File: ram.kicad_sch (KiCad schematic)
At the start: 56 parts

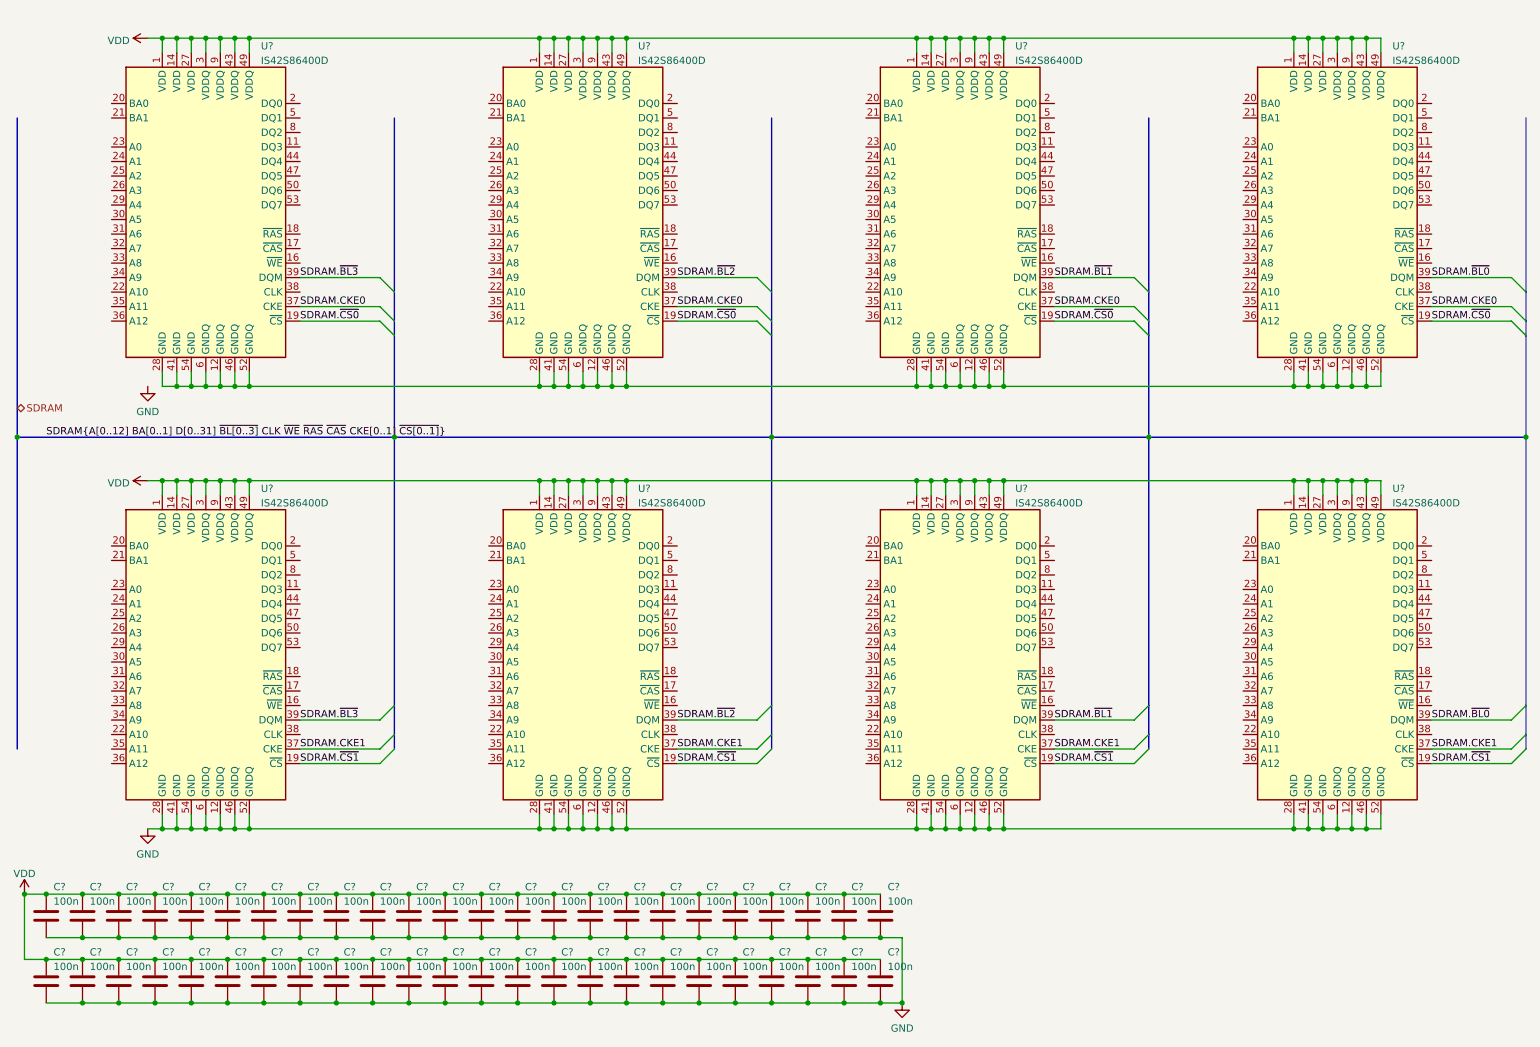
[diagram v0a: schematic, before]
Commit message: Complete wiring of SDRAM.
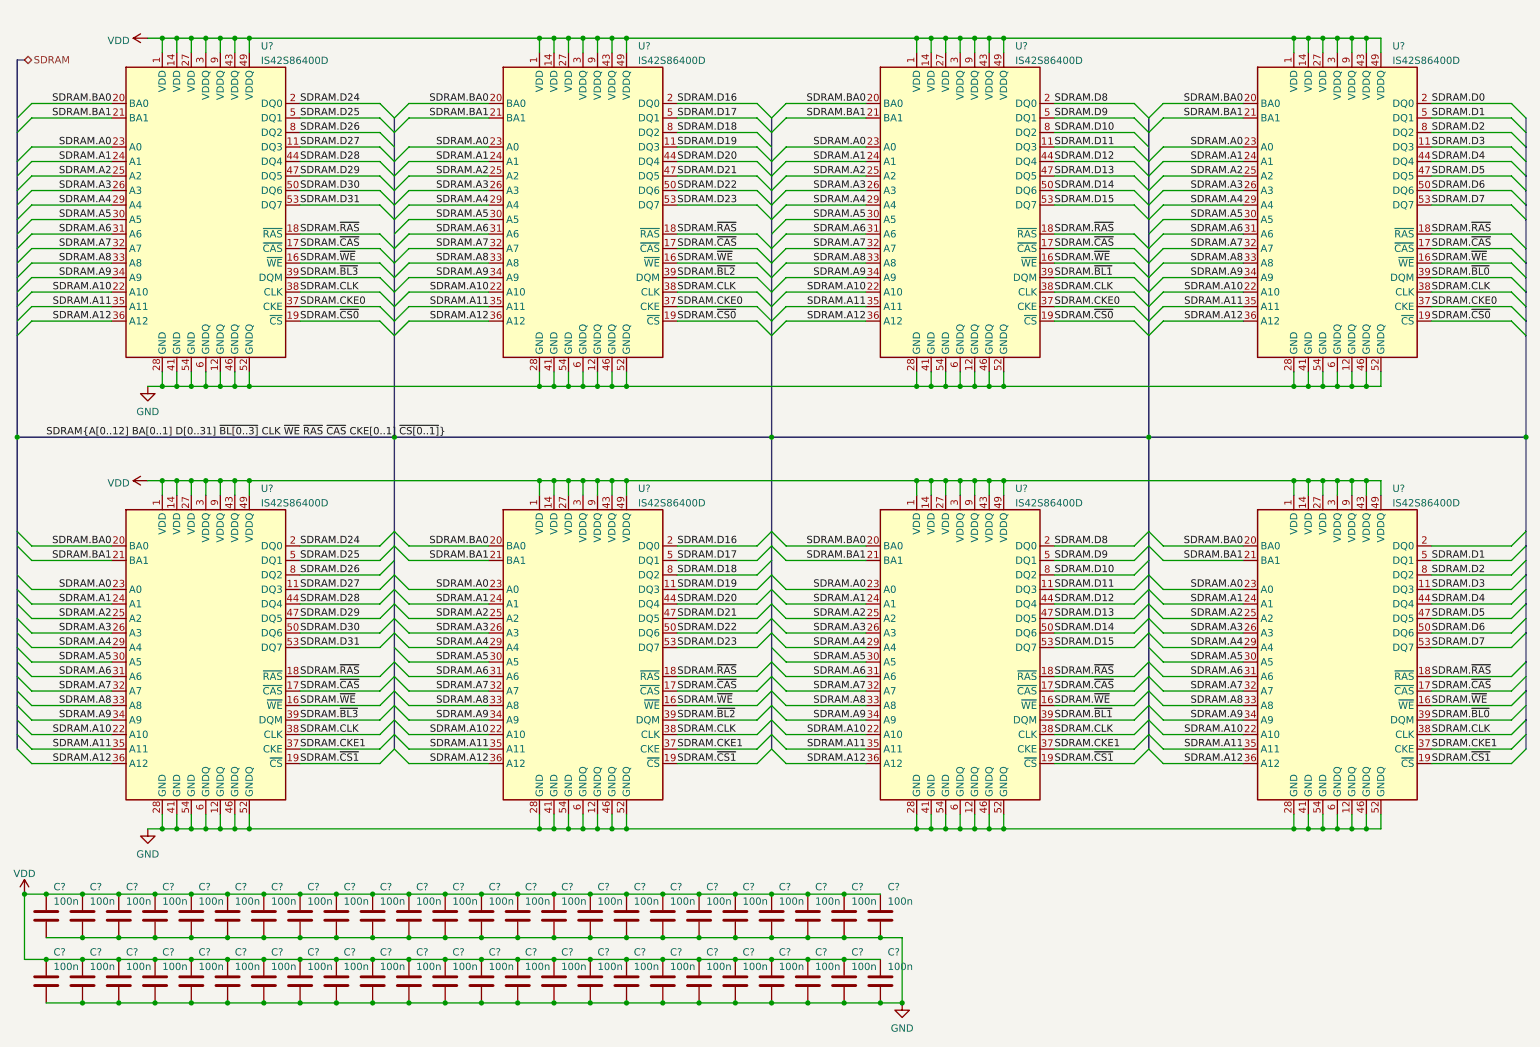
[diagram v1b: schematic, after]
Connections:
- net GND: now also U?.12 (GNDQ), U?.12 (GNDQ), U?.12 (GNDQ), U?.12 (GNDQ), U?.28 (GND), U?.28 (GND), U?.28 (GND), U?.28 (GND), U?.41 (GND), U?.41 (GND), U?.41 (GND), U?.41 (GND), U?.46 (GNDQ), U?.46 (GNDQ), U?.46 (GNDQ), U?.46 (GNDQ), U?.52 (GNDQ), U?.52 (GNDQ), U?.52 (GNDQ), U?.52 (GNDQ), U?.54 (GND), U?.54 (GND), U?.54 (GND), U?.54 (GND), U?.6 (GNDQ), U?.6 (GNDQ), U?.6 (GNDQ), U?.6 (GNDQ)
- net SDRAM.D11: now reaches U?.11 (DQ3)
- net SDRAM.D11: now also U?.11 (DQ3)
- net SDRAM.~{WE}: now reaches U?.16 (~{WE})
- net SDRAM.~{WE}: now also U?.16 (~{WE}), U?.16 (~{WE}), U?.16 (~{WE}), U?.16 (~{WE}), U?.16 (~{WE}), U?.16 (~{WE}), U?.16 (~{WE})
- net SDRAM.~{CAS}: now reaches U?.17 (~{CAS})
- net SDRAM.~{CAS}: now also U?.17 (~{CAS}), U?.17 (~{CAS}), U?.17 (~{CAS}), U?.17 (~{CAS}), U?.17 (~{CAS}), U?.17 (~{CAS}), U?.17 (~{CAS})
- net SDRAM.~{RAS}: now reaches U?.18 (~{RAS})
- net SDRAM.~{RAS}: now also U?.18 (~{RAS}), U?.18 (~{RAS}), U?.18 (~{RAS}), U?.18 (~{RAS}), U?.18 (~{RAS}), U?.18 (~{RAS}), U?.18 (~{RAS})
- net SDRAM.D8: now reaches U?.2 (DQ0)
- net SDRAM.D8: now also U?.2 (DQ0)
- net SDRAM.BA0: now reaches U?.20 (BA0)
- net SDRAM.BA0: now also U?.20 (BA0), U?.20 (BA0), U?.20 (BA0), U?.20 (BA0), U?.20 (BA0), U?.20 (BA0), U?.20 (BA0)
- net SDRAM.BA1: now reaches U?.21 (BA1)
- net SDRAM.BA1: now also U?.21 (BA1), U?.21 (BA1), U?.21 (BA1), U?.21 (BA1), U?.21 (BA1), U?.21 (BA1), U?.21 (BA1)
- net SDRAM.A10: now reaches U?.22 (A10)
- net SDRAM.A10: now also U?.22 (A10), U?.22 (A10), U?.22 (A10), U?.22 (A10), U?.22 (A10), U?.22 (A10), U?.22 (A10)
- net SDRAM.A0: now reaches U?.23 (A0)
- net SDRAM.A0: now also U?.23 (A0), U?.23 (A0), U?.23 (A0), U?.23 (A0), U?.23 (A0), U?.23 (A0), U?.23 (A0)
- net SDRAM.A1: now reaches U?.24 (A1)
- net SDRAM.A1: now also U?.24 (A1), U?.24 (A1), U?.24 (A1), U?.24 (A1), U?.24 (A1), U?.24 (A1), U?.24 (A1)
- net SDRAM.A2: now reaches U?.25 (A2)
- net SDRAM.A2: now also U?.25 (A2), U?.25 (A2), U?.25 (A2), U?.25 (A2), U?.25 (A2), U?.25 (A2), U?.25 (A2)
- net SDRAM.A3: now reaches U?.26 (A3)
- net SDRAM.A3: now also U?.26 (A3), U?.26 (A3), U?.26 (A3), U?.26 (A3), U?.26 (A3), U?.26 (A3), U?.26 (A3)
- net SDRAM.A4: now reaches U?.29 (A4)
- net SDRAM.A4: now also U?.29 (A4), U?.29 (A4), U?.29 (A4), U?.29 (A4), U?.29 (A4), U?.29 (A4), U?.29 (A4)
- net SDRAM.A5: now reaches U?.30 (A5)
- net SDRAM.A5: now also U?.30 (A5), U?.30 (A5), U?.30 (A5), U?.30 (A5), U?.30 (A5), U?.30 (A5), U?.30 (A5)
- net SDRAM.A6: now reaches U?.31 (A6)
- net SDRAM.A6: now also U?.31 (A6), U?.31 (A6), U?.31 (A6), U?.31 (A6), U?.31 (A6), U?.31 (A6), U?.31 (A6)
- net SDRAM.A7: now reaches U?.32 (A7)
- net SDRAM.A7: now also U?.32 (A7), U?.32 (A7), U?.32 (A7), U?.32 (A7), U?.32 (A7), U?.32 (A7), U?.32 (A7)
- net SDRAM.A8: now reaches U?.33 (A8)
- net SDRAM.A8: now also U?.33 (A8), U?.33 (A8), U?.33 (A8), U?.33 (A8), U?.33 (A8), U?.33 (A8), U?.33 (A8)
- net SDRAM.A9: now reaches U?.34 (A9)
- net SDRAM.A9: now also U?.34 (A9), U?.34 (A9), U?.34 (A9), U?.34 (A9), U?.34 (A9), U?.34 (A9), U?.34 (A9)
- net SDRAM.A11: now reaches U?.35 (A11)
- net SDRAM.A11: now also U?.35 (A11), U?.35 (A11), U?.35 (A11), U?.35 (A11), U?.35 (A11), U?.35 (A11), U?.35 (A11)
- net SDRAM.A12: now reaches U?.36 (A12)
- net SDRAM.A12: now also U?.36 (A12), U?.36 (A12), U?.36 (A12), U?.36 (A12), U?.36 (A12), U?.36 (A12), U?.36 (A12)
- net SDRAM.CLK: now reaches U?.38 (CLK)
- net SDRAM.CLK: now also U?.38 (CLK), U?.38 (CLK), U?.38 (CLK), U?.38 (CLK), U?.38 (CLK), U?.38 (CLK), U?.38 (CLK)
- net SDRAM.D12: now reaches U?.44 (DQ4)
- net SDRAM.D12: now also U?.44 (DQ4)
- net SDRAM.D13: now reaches U?.47 (DQ5)
- net SDRAM.D13: now also U?.47 (DQ5)
- net SDRAM.D9: now reaches U?.5 (DQ1)
- net SDRAM.D9: now also U?.5 (DQ1)
- net SDRAM.D14: now reaches U?.50 (DQ6)
- net SDRAM.D14: now also U?.50 (DQ6)
- net SDRAM.D15: now reaches U?.53 (DQ7)
- net SDRAM.D15: now also U?.53 (DQ7)
- net SDRAM.D10: now reaches U?.8 (DQ2)
- net SDRAM.D10: now also U?.8 (DQ2)
- net SDRAM.D19: now reaches U?.11 (DQ3)
- net SDRAM.D19: now also U?.11 (DQ3)
- net SDRAM.D16: now reaches U?.2 (DQ0)
- net SDRAM.D16: now also U?.2 (DQ0)
- net SDRAM.D20: now reaches U?.44 (DQ4)
- net SDRAM.D20: now also U?.44 (DQ4)
- net SDRAM.D21: now reaches U?.47 (DQ5)
- net SDRAM.D21: now also U?.47 (DQ5)
- net SDRAM.D17: now reaches U?.5 (DQ1)
- net SDRAM.D17: now also U?.5 (DQ1)
- net SDRAM.D22: now reaches U?.50 (DQ6)
- net SDRAM.D22: now also U?.50 (DQ6)
- net SDRAM.D23: now reaches U?.53 (DQ7)
- net SDRAM.D23: now also U?.53 (DQ7)
- net SDRAM.D18: now reaches U?.8 (DQ2)
- net SDRAM.D18: now also U?.8 (DQ2)
- net SDRAM.D27: now reaches U?.11 (DQ3)
- net SDRAM.D27: now also U?.11 (DQ3)
- net SDRAM.D24: now reaches U?.2 (DQ0)
- net SDRAM.D24: now also U?.2 (DQ0)
- net SDRAM.D28: now reaches U?.44 (DQ4)
- net SDRAM.D28: now also U?.44 (DQ4)
- net SDRAM.D29: now reaches U?.47 (DQ5)
- net SDRAM.D29: now also U?.47 (DQ5)
- net SDRAM.D25: now reaches U?.5 (DQ1)
- net SDRAM.D25: now also U?.5 (DQ1)
- net SDRAM.D30: now reaches U?.50 (DQ6)
- net SDRAM.D30: now also U?.50 (DQ6)
- net SDRAM.D31: now reaches U?.53 (DQ7)
- net SDRAM.D31: now also U?.53 (DQ7)
- net SDRAM.D26: now reaches U?.8 (DQ2)
- net SDRAM.D26: now also U?.8 (DQ2)
- net SDRAM.D3: now reaches U?.11 (DQ3)
- net SDRAM.D3: now also U?.11 (DQ3)
- net SDRAM.D4: now reaches U?.44 (DQ4)
- net SDRAM.D4: now also U?.44 (DQ4)
- net SDRAM.D5: now reaches U?.47 (DQ5)
- net SDRAM.D5: now also U?.47 (DQ5)
- net SDRAM.D1: now reaches U?.5 (DQ1)
- net SDRAM.D1: now also U?.5 (DQ1)
- net SDRAM.D6: now reaches U?.50 (DQ6)
- net SDRAM.D6: now also U?.50 (DQ6)
- net SDRAM.D7: now reaches U?.53 (DQ7)
- net SDRAM.D7: now also U?.53 (DQ7)
- net SDRAM.D2: now reaches U?.8 (DQ2)
- net SDRAM.D2: now also U?.8 (DQ2)
- net SDRAM.D0: now reaches U?.2 (DQ0)

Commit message: Add SD card connector.
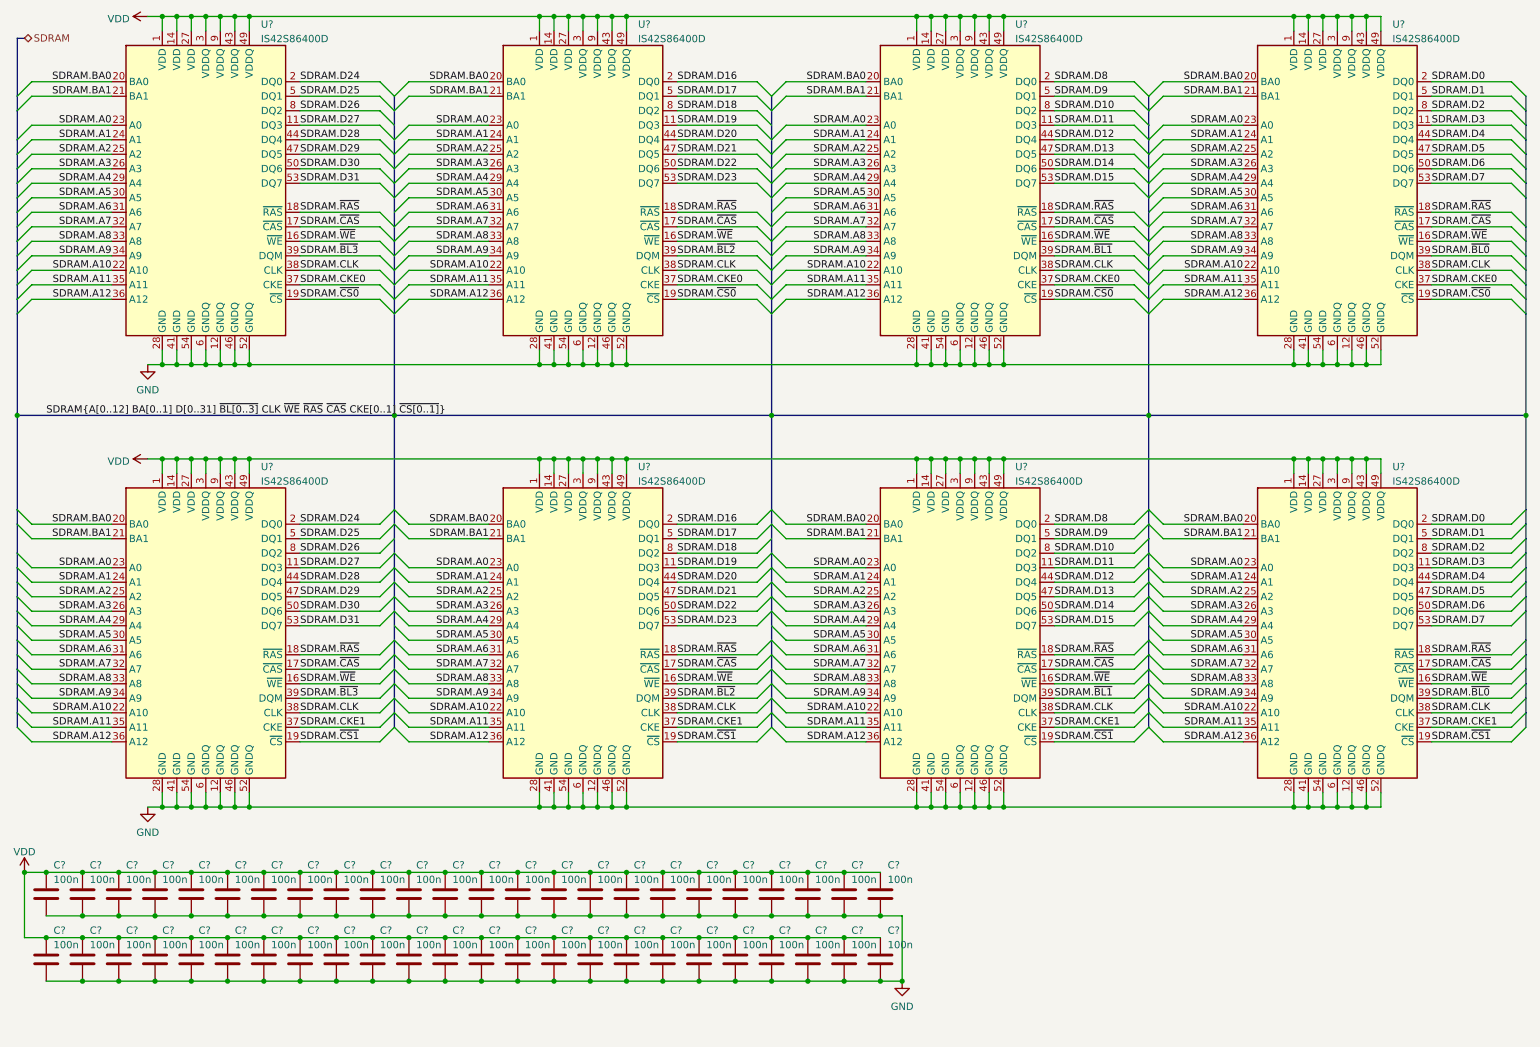
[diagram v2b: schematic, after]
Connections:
- net SDRAM.D0: now also U?.2 (DQ0)
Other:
- moved on the sheet: C?, U?

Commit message: Add power supply.
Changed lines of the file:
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@@
     (pin "2")
   )
-  (symbol (lib_id "marco-ram-board:IS42S86400D") (at 181.61 52.07 0) (unit 1)
-    (in_bom yes) (on_board yes) (fields_autoplaced)
-    (property "Reference" "U?" (id 0) (at 191.2494 21.7002 0)
-      (effects (font (size 1.27 1.27)) (justify left))
-    )
-    (property "Value" "IS42S86400D" (id 1) (at 191.2494 24.2371 0)
-      (effects (font (size 1.27 1.27)) (justify left))
-    )
+  (symbol (lib_name "IS42S86400D_4") (lib_id "marco-ram-board:IS42S86400D") (at 181.61 52.07 0) (unit 1)
+    (in_bom yes) (on_board yes)
+    (property "Reference" "U?" (id 0) (at 181.61 50.8031 0))
+    (property "Value" "IS42S86400D" (id 1) (at 181.61 53.34 0))
     (property "Footprint" "Package_SO:TSOP-II-54_22.2x10.16mm_P0.8mm" (id 2) (at 181.61 81.28 0)
       (effects (font (size 1.27 1.27)) hide)
@@
     (pin "2")
   )
-  (symbol (lib_id "marco-ram-board:IS42S86400D") (at 115.57 52.07 0) (unit 1)
-    (in_bom yes) (on_board yes) (fields_autoplaced)
-    (property "Reference" "U?" (id 0) (at 125.2094 21.7002 0)
-      (effects (font (size 1.27 1.27)) (justify left))
-    )
-    (property "Value" "IS42S86400D" (id 1) (at 125.2094 24.2371 0)
-      (effects (font (size 1.27 1.27)) (justify left))
-    )
+  (symbol (lib_name "IS42S86400D_5") (lib_id "marco-ram-board:IS42S86400D") (at 115.57 52.07 0) (unit 1)
+    (in_bom yes) (on_board yes)
+    (property "Reference" "U?" (id 0) (at 115.57 50.8 0))
+    (property "Value" "IS42S86400D" (id 1) (at 115.57 53.34 0))
     (property "Footprint" "Package_SO:TSOP-II-54_22.2x10.16mm_P0.8mm" (id 2) (at 115.57 81.28 0)
       (effects (font (size 1.27 1.27)) hide)
@@
     (pin "1")
   )
-  (symbol (lib_id "marco-ram-board:IS42S86400D") (at 49.53 129.54 0) (unit 1)
-    (in_bom yes) (on_board yes) (fields_autoplaced)
-    (property "Reference" "U?" (id 0) (at 59.1694 99.1702 0)
-      (effects (font (size 1.27 1.27)) (justify left))
-    )
-    (property "Value" "IS42S86400D" (id 1) (at 59.1694 101.7071 0)
-      (effects (font (size 1.27 1.27)) (justify left))
-    )
+  (symbol (lib_name "IS42S86400D_1") (lib_id "marco-ram-board:IS42S86400D") (at 49.53 129.54 0) (unit 1)
+    (in_bom yes) (on_board yes)
+    (property "Reference" "U?" (id 0) (at 49.53 128.2731 0))
+    (property "Value" "IS42S86400D" (id 1) (at 49.53 130.81 0))
     (property "Footprint" "Package_SO:TSOP-II-54_22.2x10.16mm_P0.8mm" (id 2) (at 49.53 158.75 0)
       (effects (font (size 1.27 1.27)) hide)
@@
   )
   (symbol (lib_id "marco-ram-board:IS42S86400D") (at 49.53 52.07 0) (unit 1)
-    (in_bom yes) (on_board yes) (fields_autoplaced)
-    (property "Reference" "U?" (id 0) (at 59.1694 21.7002 0)
-      (effects (font (size 1.27 1.27)) (justify left))
-    )
-    (property "Value" "IS42S86400D" (id 1) (at 59.1694 24.2371 0)
-      (effects (font (size 1.27 1.27)) (justify left))
-    )
+    (in_bom yes) (on_board yes)
+    (property "Reference" "U?" (id 0) (at 49.53 50.8031 0))
+    (property "Value" "IS42S86400D" (id 1) (at 49.53 53.34 0))
     (property "Footprint" "Package_SO:TSOP-II-54_22.2x10.16mm_P0.8mm" (id 2) (at 49.53 81.28 0)
       (effects (font (size 1.27 1.27)) hide)
@@
     (pin "2")
   )
-  (symbol (lib_id "marco-ram-board:IS42S86400D") (at 247.65 129.54 0) (unit 1)
-    (in_bom yes) (on_board yes) (fields_autoplaced)
-    (property "Reference" "U?" (id 0) (at 257.2894 99.1702 0)
-      (effects (font (size 1.27 1.27)) (justify left))
-    )
-    (property "Value" "IS42S86400D" (id 1) (at 257.2894 101.7071 0)
-      (effects (font (size 1.27 1.27)) (justify left))
-    )
+  (symbol (lib_name "IS42S86400D_6") (lib_id "marco-ram-board:IS42S86400D") (at 247.65 129.54 0) (unit 1)
+    (in_bom yes) (on_board yes)
+    (property "Reference" "U?" (id 0) (at 247.65 128.2731 0))
+    (property "Value" "IS42S86400D" (id 1) (at 247.65 130.81 0))
     (property "Footprint" "Package_SO:TSOP-II-54_22.2x10.16mm_P0.8mm" (id 2) (at 247.65 158.75 0)
       (effects (font (size 1.27 1.27)) hide)
@@
     (pin "2")
   )
-  (symbol (lib_id "marco-ram-board:IS42S86400D") (at 247.65 52.07 0) (unit 1)
-    (in_bom yes) (on_board yes) (fields_autoplaced)
-    (property "Reference" "U?" (id 0) (at 257.2894 21.7002 0)
-      (effects (font (size 1.27 1.27)) (justify left))
-    )
-    (property "Value" "IS42S86400D" (id 1) (at 257.2894 24.2371 0)
-      (effects (font (size 1.27 1.27)) (justify left))
-    )
+  (symbol (lib_name "IS42S86400D_3") (lib_id "marco-ram-board:IS42S86400D") (at 247.65 52.07 0) (unit 1)
+    (in_bom yes) (on_board yes)
+    (property "Reference" "U?" (id 0) (at 247.65 50.8031 0))
+    (property "Value" "IS42S86400D" (id 1) (at 247.65 53.34 0))
     (property "Footprint" "Package_SO:TSOP-II-54_22.2x10.16mm_P0.8mm" (id 2) (at 247.65 81.28 0)
       (effects (font (size 1.27 1.27)) hide)
@@
     (pin "1")
   )
-  (symbol (lib_id "marco-ram-board:IS42S86400D") (at 115.57 129.54 0) (unit 1)
-    (in_bom yes) (on_board yes) (fields_autoplaced)
-    (property "Reference" "U?" (id 0) (at 125.2094 99.1702 0)
-      (effects (font (size 1.27 1.27)) (justify left))
-    )
-    (property "Value" "IS42S86400D" (id 1) (at 125.2094 101.7071 0)
-      (effects (font (size 1.27 1.27)) (justify left))
-    )
+  (symbol (lib_name "IS42S86400D_7") (lib_id "marco-ram-board:IS42S86400D") (at 115.57 129.54 0) (unit 1)
+    (in_bom yes) (on_board yes)
+    (property "Reference" "U?" (id 0) (at 115.57 128.2731 0))
+    (property "Value" "IS42S86400D" (id 1) (at 115.57 130.81 0))
     (property "Footprint" "Package_SO:TSOP-II-54_22.2x10.16mm_P0.8mm" (id 2) (at 115.57 158.75 0)
       (effects (font (size 1.27 1.27)) hide)
@@
     (pin "2")
   )
-  (symbol (lib_id "marco-ram-board:IS42S86400D") (at 181.61 129.54 0) (unit 1)
-    (in_bom yes) (on_board yes) (fields_autoplaced)
-    (property "Reference" "U?" (id 0) (at 191.2494 99.1702 0)
-      (effects (font (size 1.27 1.27)) (justify left))
-    )
-    (property "Value" "IS42S86400D" (id 1) (at 191.2494 101.7071 0)
-      (effects (font (size 1.27 1.27)) (justify left))
-    )
+  (symbol (lib_name "IS42S86400D_2") (lib_id "marco-ram-board:IS42S86400D") (at 181.61 129.54 0) (unit 1)
+    (in_bom yes) (on_board yes)
+    (property "Reference" "U?" (id 0) (at 181.61 128.2731 0))
+    (property "Value" "IS42S86400D" (id 1) (at 181.61 130.81 0))
     (property "Footprint" "Package_SO:TSOP-II-54_22.2x10.16mm_P0.8mm" (id 2) (at 181.61 158.75 0)
       (effects (font (size 1.27 1.27)) hide)
